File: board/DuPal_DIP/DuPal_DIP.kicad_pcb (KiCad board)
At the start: 2 copper layers, 51 parts, among them J1 AVR-ISP-6, J2 RS232, J3 Power IN, SW1 SW_Push, SW2 Power, U1 ATmega8A-PU, U10 24 Pin PAL, U2 74HC595, U3 74HC595, U5 20 Pin PAL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

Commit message: First PCB model for Rev.2
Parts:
- added G***: LOGO, logo:logo, F.Cu at (205.7, 86.4)
- added H1: MountingHole_Pad, MountingHole:MountingHole_2.7mm_M2.5_ISO7380_Pad, F.Cu at (95.2, 58.4)
- added H2: MountingHole_Pad, MountingHole:MountingHole_2.7mm_M2.5_ISO7380_Pad, F.Cu at (200.7, 58.4)
- added H3: MountingHole_Pad, MountingHole:MountingHole_2.7mm_M2.5_ISO7380_Pad, F.Cu at (95.2, 129.5)
- added H4: MountingHole_Pad, MountingHole:MountingHole_2.7mm_M2.5_ISO7380_Pad, F.Cu at (200.7, 129.5)
- moved C14 115.8 mm to (158.8, 59.7)
- moved J3 110.1 mm to (190.5, 64.8)
- moved D2 90.2 mm to (196.8, 73.7)
- moved SW2 85.0 mm to (176.5, 59.7), turned to 180 degrees
- moved R17 75.0 mm to (194.3, 68.6), turned to 180 degrees
- moved J2 74.0 mm to (110.5, 59.7)
- moved C3 71.5 mm to (130.8, 71.1)
- moved C4 71.5 mm to (109.2, 80.0)
- moved C5 71.5 mm to (115.6, 80.0)
- moved C7 71.5 mm to (123.2, 81.3)
- moved U6 71.5 mm to (108.0, 73.7)
- moved J1 70.3 mm to (99.1, 99.1)
- moved C6 70.3 mm to (100.3, 71.1)
- moved R2 68.1 mm to (198.1, 110.5)
- moved R4 68.1 mm to (190.5, 115.6)
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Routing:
- net GND: track 0.00 -> 453.3 mm
- net VCC: track 0.00 -> 315.3 mm
- net /P20_12: track 0.00 -> 136.2 mm, vias 0 -> 1
- net /~RESET: track 0.00 -> 135.6 mm
- net /SIPO_O_7: track 0.00 -> 131.0 mm, vias 0 -> 1
- net /SIPO_O_12: track 0.00 -> 124.0 mm, vias 0 -> 1
- net Net-(D5-Pad2): track 0.00 -> 113.5 mm, vias 0 -> 1
- net /SIPO_O_8: track 0.00 -> 112.4 mm
- net /P20_13: track 0.00 -> 110.8 mm, vias 0 -> 2
- net /SIPO_O_14: track 0.00 -> 109.7 mm, vias 0 -> 1
- net /SIPO_O_13: track 0.00 -> 109.3 mm, vias 0 -> 2
- net /SIPO_O_11: track 0.00 -> 106.2 mm, vias 0 -> 1
- net /SIPO_O_10: track 0.00 -> 101.9 mm, vias 0 -> 1
- net Net-(D4-Pad2): track 0.00 -> 100.3 mm, vias 0 -> 1
- net /P24_11: track 0.00 -> 99.7 mm, vias 0 -> 2
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- added copper zone on B.Cu, net GND
- added copper zone on F.Cu, net GND
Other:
- board outline added: 113 x 78.7 mm
- board text added: "20 PINs PAL"
- board text added: "24 PINs PAL"
- board text removed: "Put PAL here"

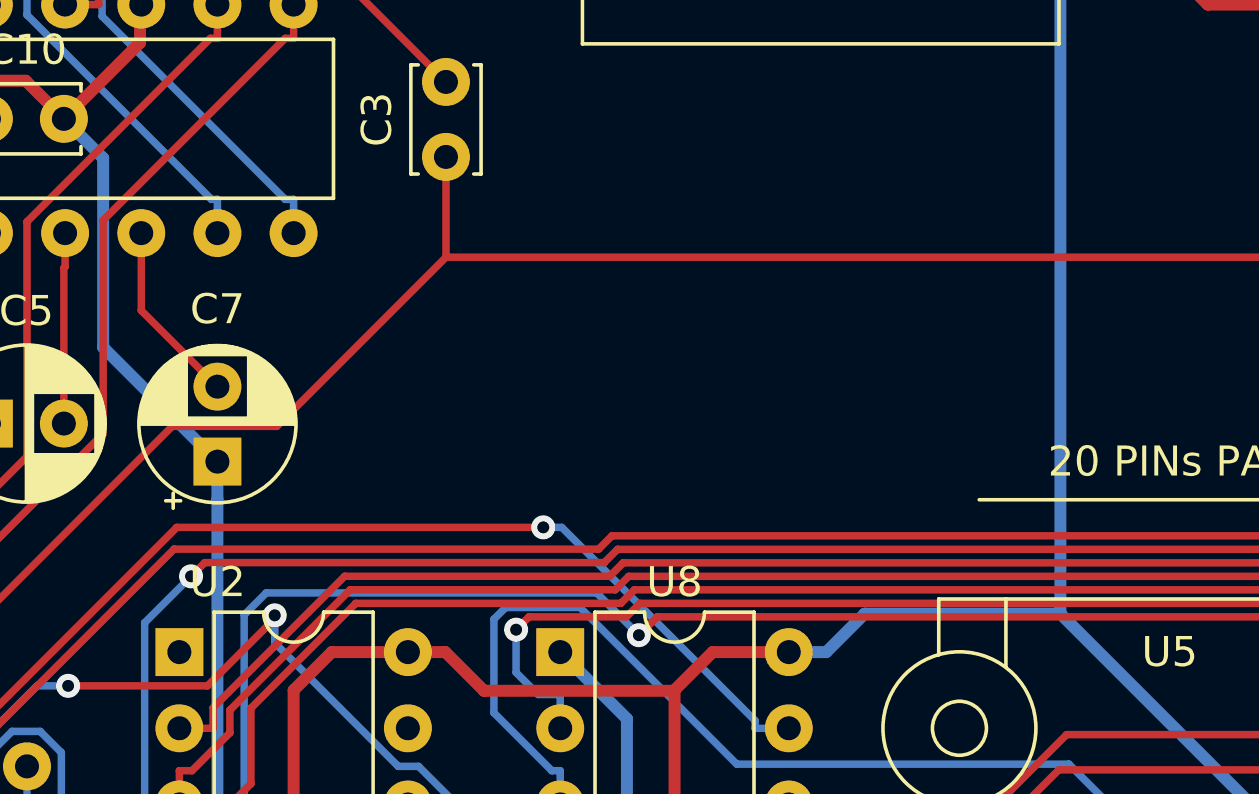
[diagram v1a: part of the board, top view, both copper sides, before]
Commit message: Add some silkscreen changes
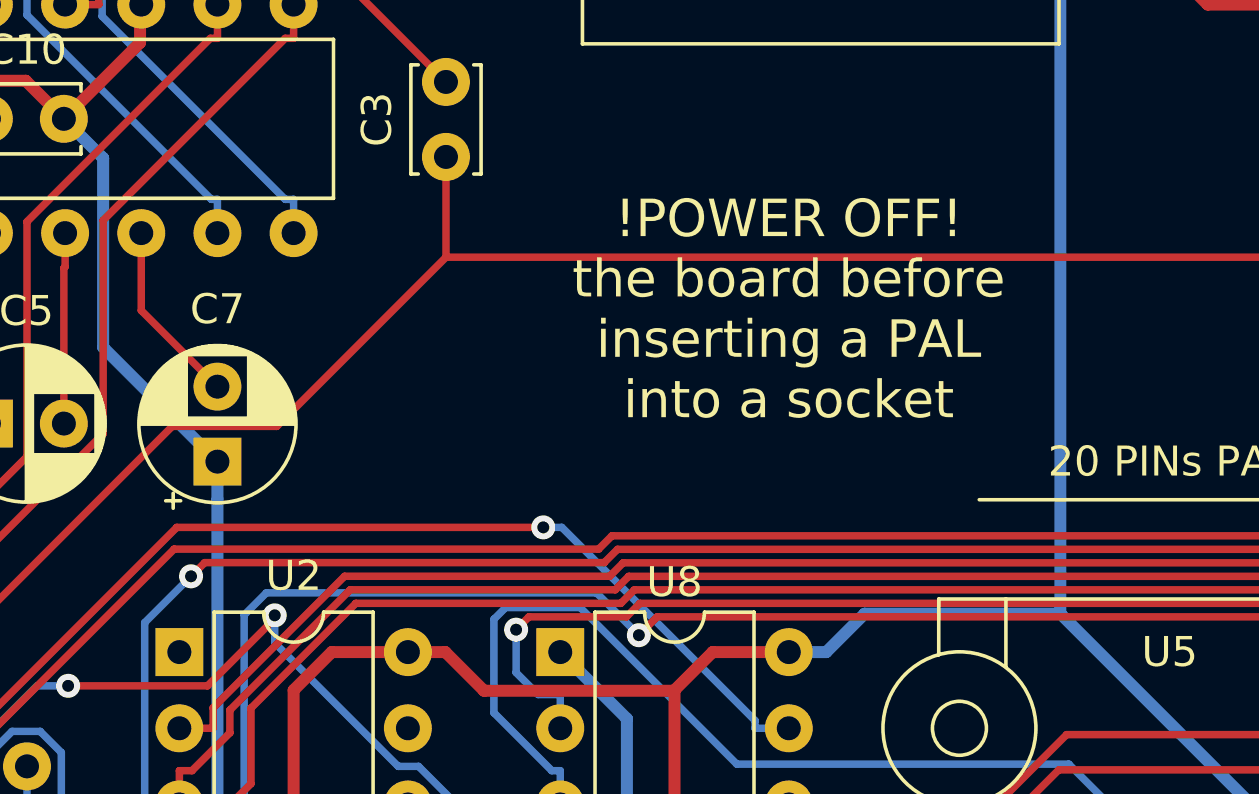
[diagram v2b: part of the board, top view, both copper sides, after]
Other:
- board text added: "!POWER OFF! the board before inserting a PAL into a socket"
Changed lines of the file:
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@@
   (general
     (thickness 1.6)
-    (drawings 24)
+    (drawings 25)
     (tracks 1097)
     (zones 0)
@@
   (page A4)
   (layers
-    (0 F.Cu signal)
-    (31 B.Cu signal)
+    (0 F.Cu signal hide)
+    (31 B.Cu signal hide)
     (32 B.Adhes user)
     (33 F.Adhes user)
@@
     (descr "16-lead though-hole mounted DIP package, row spacing 7.62 mm (300 mils)")
     (tags "THT DIP DIL PDIP 2.54mm 7.62mm 300mil")
-    (fp_text reference U2 (at 1.27 -2.33) (layer F.SilkS)
+    (fp_text reference U2 (at 3.81 -2.54) (layer F.SilkS)
       (effects (font (size 1 1) (thickness 0.15)))
     )
@@
     )
   )
+  (gr_text "!POWER OFF!\nthe board before\ninserting a PAL\ninto a socket" (at 142.24 76.2) (layer F.SilkS)
+    (effects (font (size 1.25 1.25) (thickness 0.15)))
+  )
   (gr_line (start 180.34 77.47) (end 181.61 78.74) (layer F.SilkS) (width 0.12))

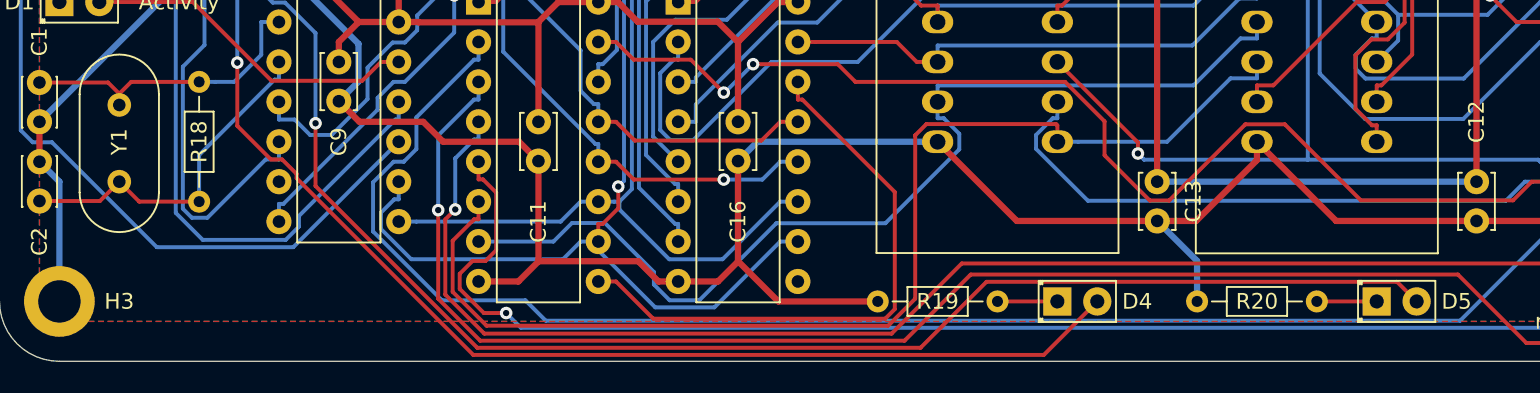
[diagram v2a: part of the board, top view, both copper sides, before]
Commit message: More silkscreen changes
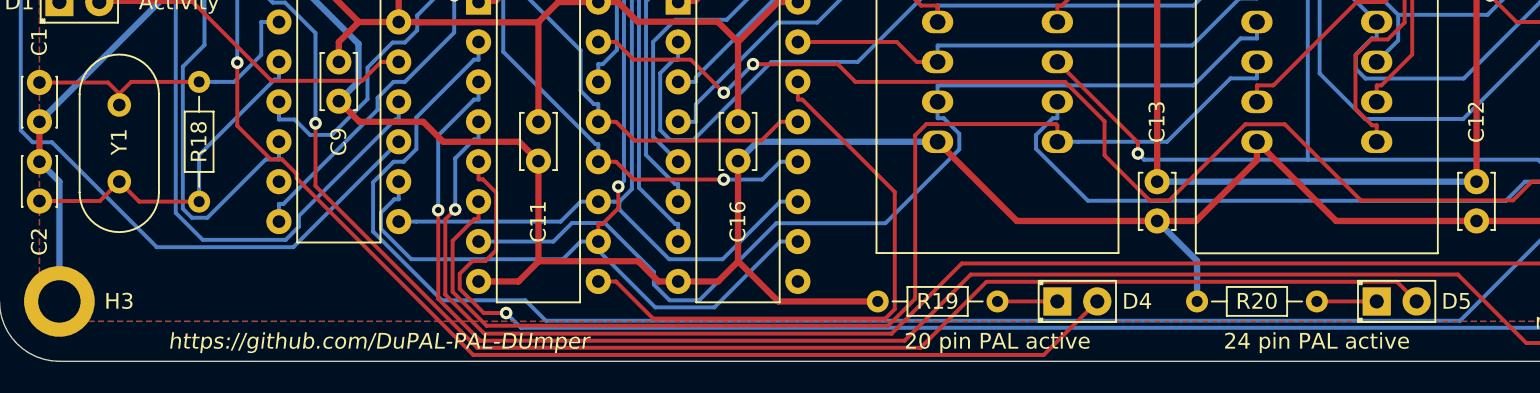
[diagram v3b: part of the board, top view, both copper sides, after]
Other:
- board text added: "20 pin PAL active"
- board text added: "24 pin PAL active"
- board text added: "https://github.com/DuPAL-PAL-DUmper"
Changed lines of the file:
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@@
   (general
     (thickness 1.6)
-    (drawings 25)
+    (drawings 28)
     (tracks 1097)
     (zones 0)
@@
     (descr "C, Disc series, Radial, pin pitch=2.50mm, , diameter*width=3.4*2.1mm^2, Capacitor, http://www.vishay.com/docs/45233/krseries.pdf")
     (tags "C Disc series Radial pin pitch 2.50mm  diameter 3.4mm width 2.1mm Capacitor")
-    (fp_text reference C13 (at 1.25 -2.3 90) (layer F.SilkS)
+    (fp_text reference C13 (at -3.81 0 90) (layer F.SilkS)
       (effects (font (size 1 1) (thickness 0.15)))
     )
@@
     )
   )
+  (gr_text https://github.com/DuPAL-PAL-DUmper (at 115.57 132.08) (layer F.SilkS)
+    (effects (font (size 1 1) (thickness 0.15) italic))
+  )
+  (gr_text "24 pin PAL active" (at 175.26 132.08) (layer F.SilkS)
+    (effects (font (size 1 1) (thickness 0.15)))
+  )
+  (gr_text "20 pin PAL active" (at 154.94 132.08) (layer F.SilkS)
+    (effects (font (size 1 1) (thickness 0.15)))
+  )
   (gr_text "!POWER OFF!\nthe board before\ninserting a PAL\ninto a socket" (at 142.24 76.2) (layer F.SilkS)
